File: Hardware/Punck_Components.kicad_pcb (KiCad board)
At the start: 4 copper layers, 91.2 x 100 mm, 114 parts, among them J1 Conn_01x12_Female, J2 Conn_01x12_Female, J3 Conn_01x12_Female, J4 Conn_01x12_Female, J5 Debug_Header, J6 SWD_Header, J7 Eurorack_10_pin_power, Q1 MMBT3904, Q2 MMBT3904, Q3 MMBT3904, Q4 MMBT3904, Q5 MMBT3904, Q6 MMBT3904, Q7 MMBT3904, U1 TL074, U2 STM32H743ZITx, U3 W25Q128JVS, U4 PCM5100APW, U5 W25Q128JVS, U6 TPS561201, U7 LD1117-3.3-4Tab, Y1 8MHz 20pF

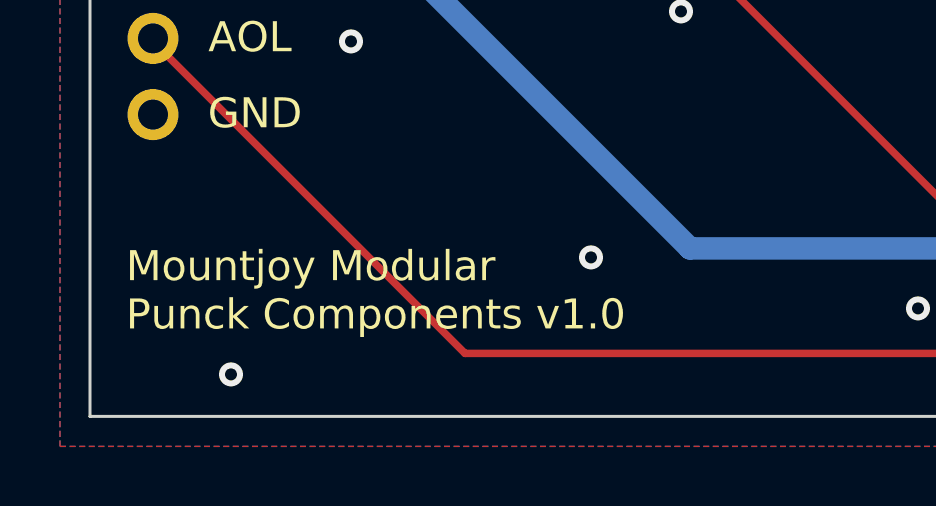
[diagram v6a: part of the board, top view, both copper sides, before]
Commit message: Fixes to copper pour on L2 for v1 production
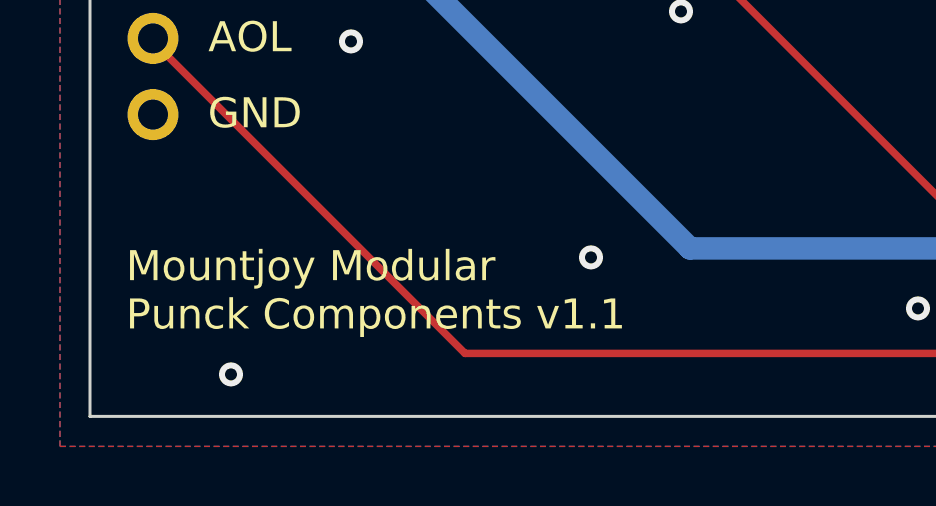
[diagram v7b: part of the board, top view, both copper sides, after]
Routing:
- added copper zone on In1.Cu, net GND
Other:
- board text added: "Mountjoy Modular Punck Components v1.1"
- board text removed: "Mountjoy Modular Punck Components v1.0"
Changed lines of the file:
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@@
     (effects (font (size 1 1) (thickness 0.15)))
   )
-  (gr_text "Mountjoy Modular\nPunck Components v1.0" (at 71.2 145.8) (layer "F.SilkS")
+  (gr_text "Mountjoy Modular\nPunck Components v1.1" (at 71.2 145.8) (layer "F.SilkS")
     (effects (font (size 1 1) (thickness 0.2)) (justify left))
   )
@@
   (segment (start 129.175 86.6) (end 128.725 87.05) (width 0.25) (layer "F.Cu") (net 161))
   (segment (start 128.725 87.05) (end 126.2625 87.05) (width 0.25) (layer "F.Cu") (net 161))
-  (zone locked (net 10) (net_name "GND") (layers "F.Cu" "In2.Cu" "B.Cu") (hatch edge 0.508)
+  (zone locked (net 10) (net_name "GND") (layers "F.Cu" "In1.Cu" "In2.Cu" "B.Cu") (hatch edge 0.508)
     (connect_pads (clearance 0.508))
     (min_thickness 0.254) (filled_areas_thickness no)
@@
   )
   (zone (net 46) (net_name "/VSW") (layer "In1.Cu") (hatch edge 0.508)
+    (priority 1)
     (connect_pads (clearance 0.508))
     (min_thickness 0.254) (filled_areas_thickness no)

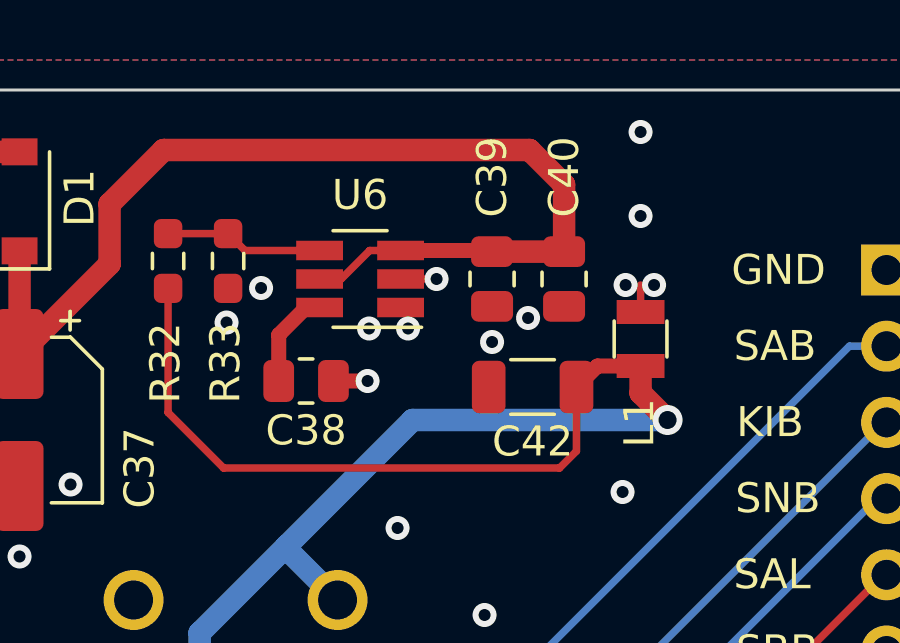
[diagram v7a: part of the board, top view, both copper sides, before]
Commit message: Started altering project to bring up v1 hardware
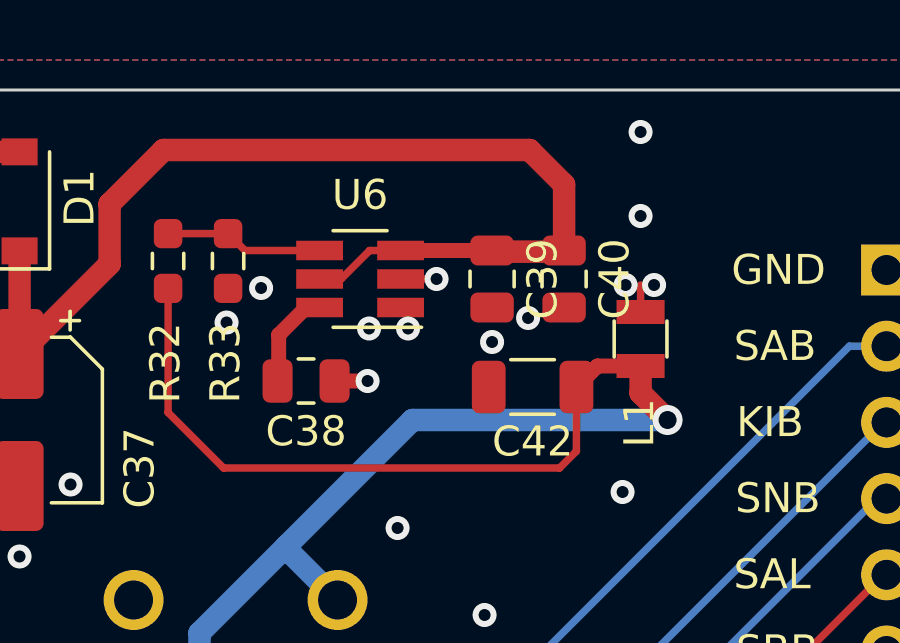
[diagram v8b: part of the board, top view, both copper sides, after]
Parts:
- C38, C39, C40: footprint Resistor_SMD:R_0805_2012Metric -> Capacitor_SMD:C_0805_2012Metric
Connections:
- net Net-(JP1-Pad2) renamed /QSPI2_NCS
